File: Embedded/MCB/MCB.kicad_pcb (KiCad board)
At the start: 2 copper layers, 19.2 x 33 mm, 23 parts, among them J1 USB, J2 Power, J3 MicroSD, J4 GPIO Pair 0, J5 GPIO Pair 1, U1 Sensored, U2 Expansion, U3 Comms Link Expansion, U4 AP7366-33W5-7

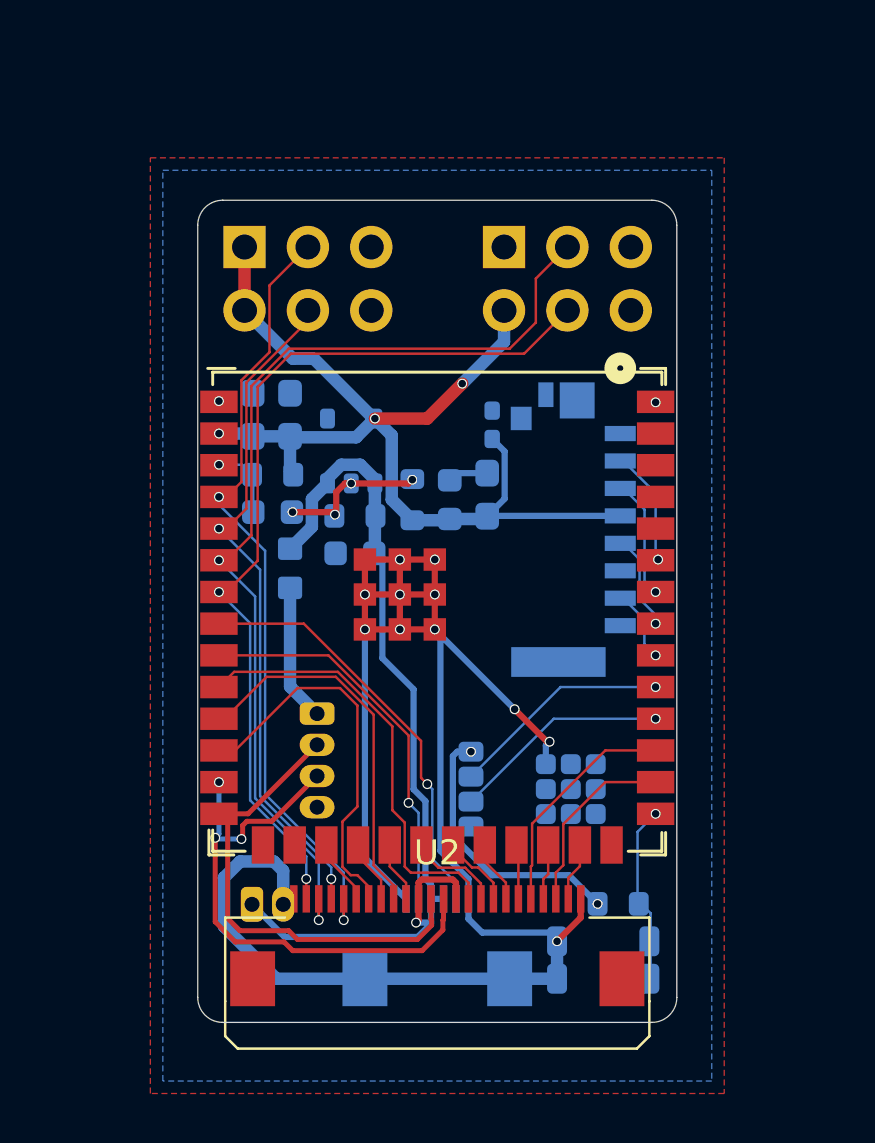
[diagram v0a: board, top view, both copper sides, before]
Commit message: Added USB-2WComms Solder Bridge
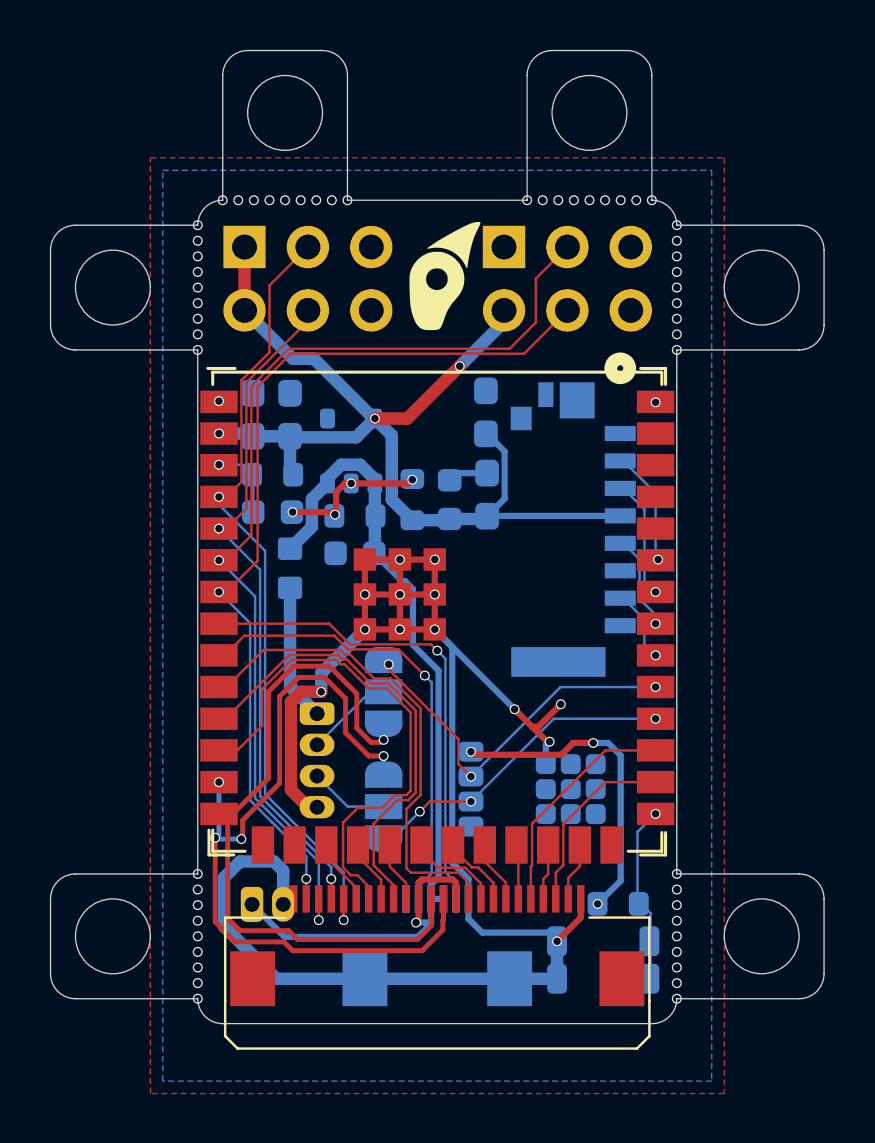
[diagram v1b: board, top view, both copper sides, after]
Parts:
- added JP1: USB +, Jumper:SolderJumper-3_P1.3mm_Open_RoundedPad1.0x1.5mm, B.Cu at (137.8, 102.9)
- added JP2: USB -, Jumper:SolderJumper-3_P1.3mm_Open_RoundedPad1.0x1.5mm, B.Cu at (137.8, 107.5)
- added REF**: Logo_5mm, Logo:Logo_5mm, F.Cu at (140.0, 86.3)
- C10: footprint Capacitor_SMD:C_0402_1005Metric_Pad0.74x0.62mm_HandSolder -> Capacitor_SMD:C_0603_1608Metric_Pad1.08x0.95mm_HandSolder
- moved C10 0.56 mm to (141.9, 91.7)
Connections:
- net EXP UART RX renamed EXP Comms B
- net EXP UART TX renamed EXP Comms A
- J1 pad 2: USB + -> Net-(J1-Pin_2)
- J1 pad 3: USB - -> Net-(J1-Pin_3)
- U3 pad : GND -> (no net)
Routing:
- net USB -: track 22.3 -> 31.6 mm, vias 3 -> 4
- net USB +: track 19.2 -> 28.0 mm, vias 0 -> 1
- net Sensor SDA: track 8.93 -> 15.1 mm, vias 1 -> 3
- net Exp 1: track 15.5 -> 20.9 mm
- net Sensor SCL: track 8.78 -> 12.9 mm, vias 1 -> 3
- net Net-(J1-Pin_2): track 0.00 -> 3.55 mm
- net Exp 3: track 15.2 -> 18.7 mm
- net Net-(J1-Pin_3): track 0.00 -> 3.17 mm
- net EXP Comms B: track 15.6 -> 18.5 mm
- net EXP Comms A: track 17.0 -> 19.5 mm
- net Exp 5: track 17.4 -> 19.7 mm
- net +3V3: track 53.1 -> 54.5 mm, vias 5 -> 6
- net GND: track 83.3 -> 82.8 mm, vias 17 -> 19
- net (no net): vias 0 -> 54
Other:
- board size 19.2 x 33 mm -> 31 x 39 mm

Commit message: Modified Some Traces for Lower Noise
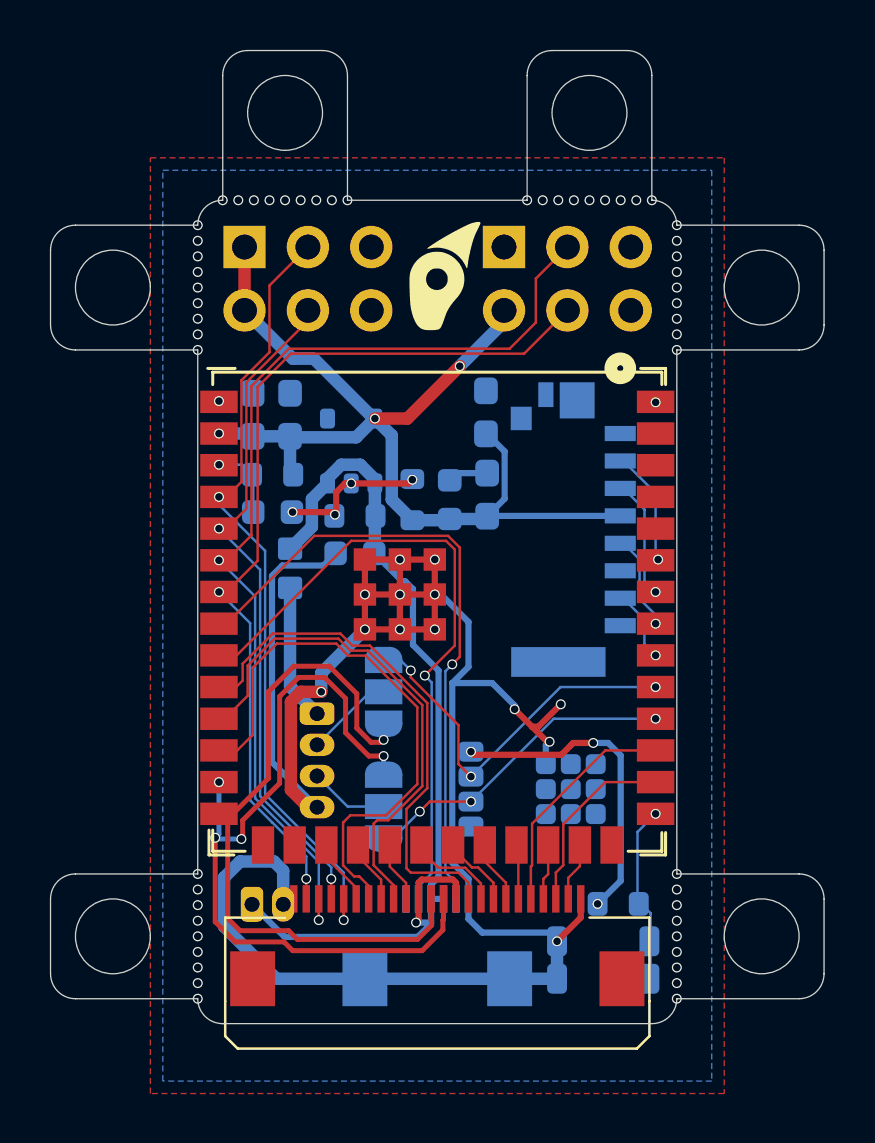
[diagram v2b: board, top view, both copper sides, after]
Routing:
- net GND: track 82.8 -> 96.3 mm
- net EXP Comms B: track 18.5 -> 26.3 mm
- net EXP Comms A: track 19.5 -> 25.8 mm
- net Exp 3: track 18.7 -> 20.5 mm
- net Exp 1: track 20.9 -> 22.7 mm
- net Exp 5: track 19.7 -> 21.1 mm
